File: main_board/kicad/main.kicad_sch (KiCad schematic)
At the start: 13 parts

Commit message: started bridge design
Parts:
- removed C? (x3): C, symbol Device:C
- removed D?: 1N5822, Diode_THT:D_DO-201AD_P15.24mm_Horizontal, symbol Diode:1N5822
- removed L?: L, symbol Device:L
- removed Q?: IRFB3077, Package_TO_SOT_THT:TO-220-3_Vertical, symbol 2022-lsd:IRFB3077
- removed R? (x3): R, symbol Device:R
- removed U?: LM2576S-5, Package_TO_SOT_SMD:TO-263-5_TabPin3, symbol Regulator_Switching:LM2576S-5
- removed U?: IR2133, Package_DIP:DIP-28_W15.24mm, symbol Driver_FET:IR2133
- removed U?: ATtiny13-20P, Package_DIP:DIP-8_W7.62mm, symbol MCU_Microchip_ATtiny:ATtiny13-20P
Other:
- added sheet attiny13 (attiny13.kicad_sch)
- added sheet bridge (bridge.kicad_sch)
- added sheet stepDown-24-5 (stepDown-24-5.kicad_sch)

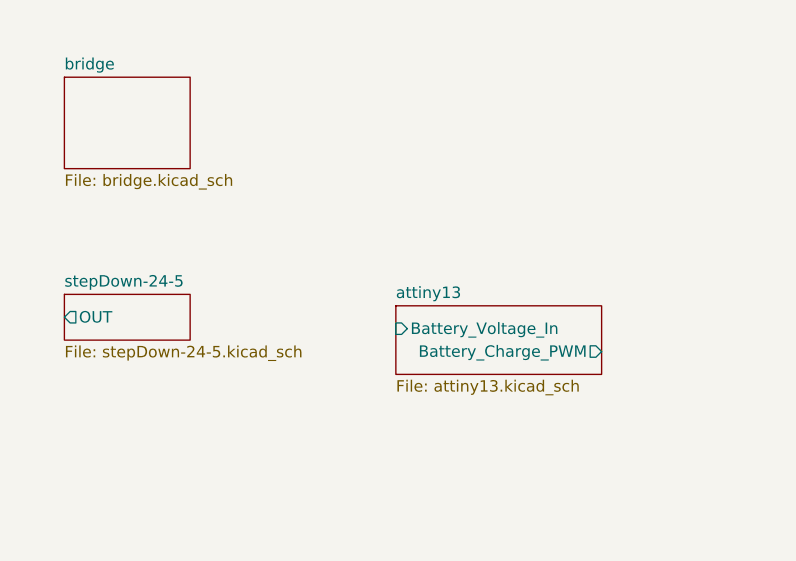
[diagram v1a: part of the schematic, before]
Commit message: changes to bridge design
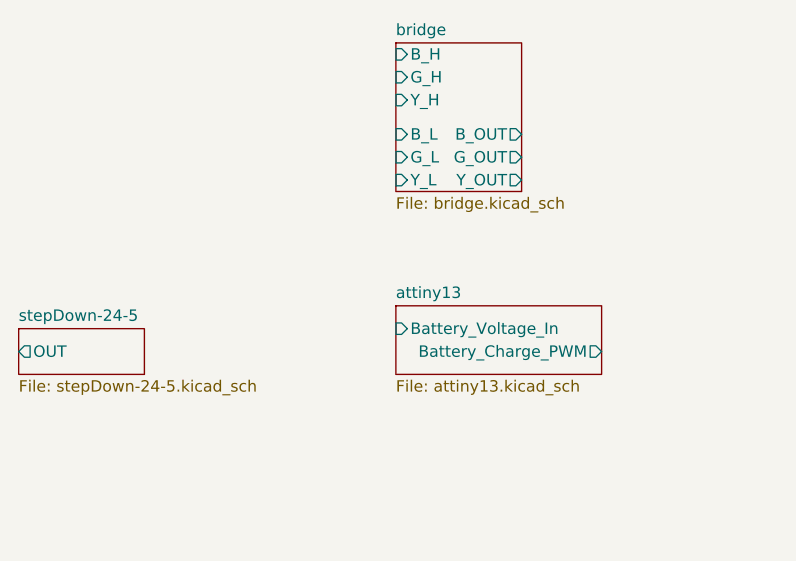
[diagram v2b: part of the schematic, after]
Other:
- sheet bridge ports: added B_H, B_L, B_OUT, G_H, G_L, G_OUT, Y_H, Y_L, Y_OUT; removed none
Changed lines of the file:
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@@
     )
   )
-  (sheet (at 163.83 156.21) (size 13.97 10.16) (fields_autoplaced)
+  (sheet (at 200.66 152.4) (size 13.97 16.51) (fields_autoplaced)
     (stroke (width 0.1524) (type solid))
     (fill (color 0 0 0 0.0000))
-    (property "Sheetname" "bridge" (at 163.83 155.4984 0)
+    (property "Sheetname" "bridge" (at 200.66 151.6884 0)
       (effects (font (size 1.27 1.27)) (justify left bottom))
     )
-    (property "Sheetfile" "bridge.kicad_sch" (at 163.83 166.9546 0)
+    (property "Sheetfile" "bridge.kicad_sch" (at 200.66 169.4946 0)
       (effects (font (size 1.27 1.27)) (justify left top))
+    )
+    (pin "G_H" input (at 200.66 156.21 180)
+      (effects (font (size 1.27 1.27)) (justify left))
+    )
+    (pin "Y_L" input (at 200.66 167.64 180)
+      (effects (font (size 1.27 1.27)) (justify left))
+    )
+    (pin "Y_OUT" output (at 214.63 167.64 0)
+      (effects (font (size 1.27 1.27)) (justify right))
+    )
+    (pin "Y_H" input (at 200.66 158.75 180)
+      (effects (font (size 1.27 1.27)) (justify left))
+    )
+    (pin "G_OUT" output (at 214.63 165.1 0)
+      (effects (font (size 1.27 1.27)) (justify right))
+    )
+    (pin "G_L" input (at 200.66 165.1 180)
+      (effects (font (size 1.27 1.27)) (justify left))
+    )
+    (pin "B_L" input (at 200.66 162.56 180)
+      (effects (font (size 1.27 1.27)) (justify left))
+    )
+    (pin "B_OUT" output (at 214.63 162.56 0)
+      (effects (font (size 1.27 1.27)) (justify right))
+    )
+    (pin "B_H" input (at 200.66 153.67 180)
+      (effects (font (size 1.27 1.27)) (justify left))
     )
     (instances
@@
     )
   )
-  (sheet (at 163.83 180.34) (size 13.97 5.08) (fields_autoplaced)
+  (sheet (at 158.75 184.15) (size 13.97 5.08) (fields_autoplaced)
     (stroke (width 0.1524) (type solid))
     (fill (color 0 0 0 0.0000))
-    (property "Sheetname" "stepDown-24-5" (at 163.83 179.6284 0)
+    (property "Sheetname" "stepDown-24-5" (at 158.75 183.4384 0)
       (effects (font (size 1.27 1.27)) (justify left bottom))
     )
-    (property "Sheetfile" "stepDown-24-5.kicad_sch" (at 163.83 186.0046 0)
+    (property "Sheetfile" "stepDown-24-5.kicad_sch" (at 158.75 189.8146 0)
       (effects (font (size 1.27 1.27)) (justify left top))
     )
-    (pin "OUT" output (at 163.83 182.88 180)
+    (pin "OUT" output (at 158.75 186.69 180)
       (effects (font (size 1.27 1.27)) (justify left))
     )

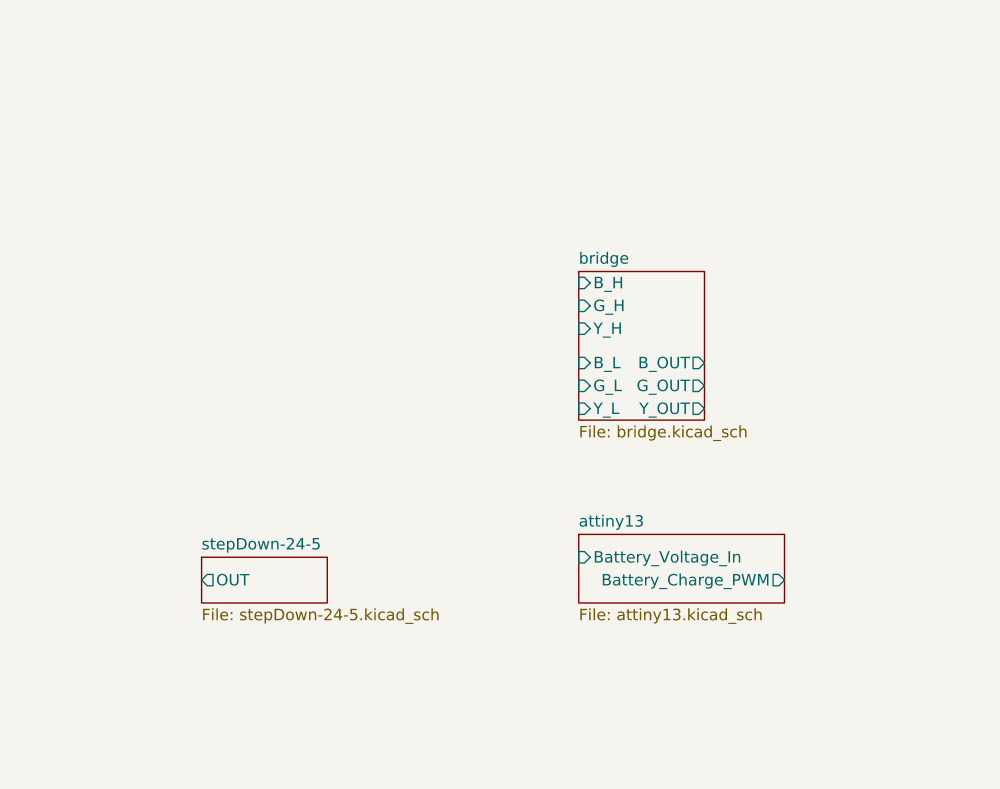
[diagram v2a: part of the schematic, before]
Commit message: added bridge driver stub
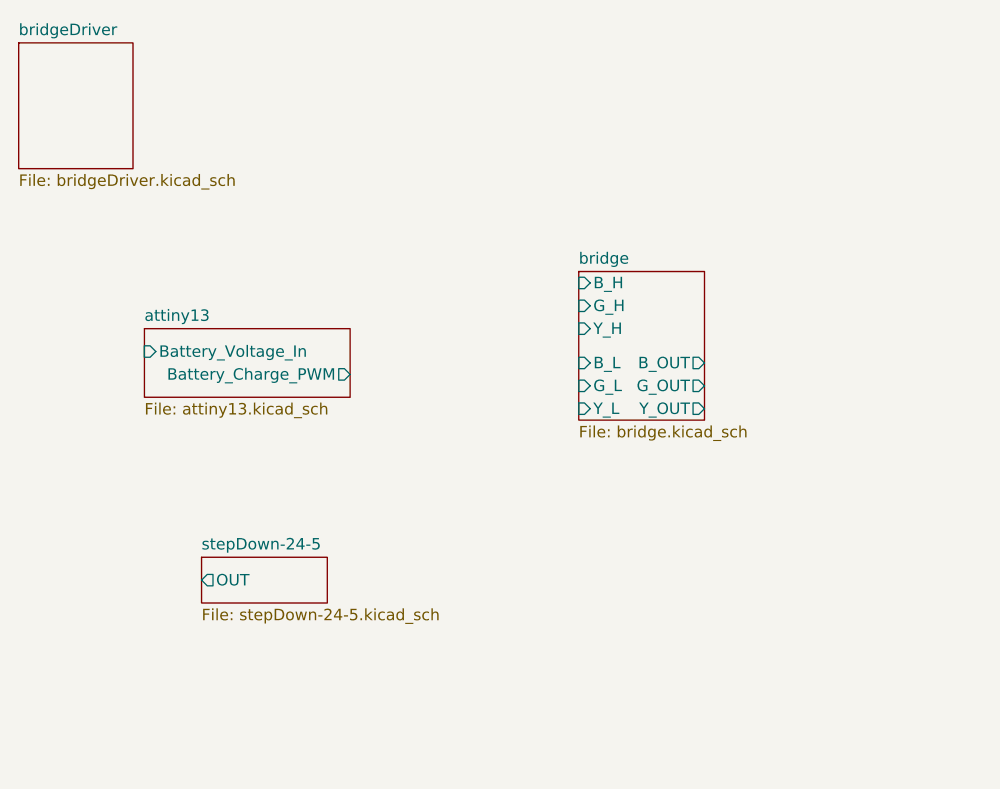
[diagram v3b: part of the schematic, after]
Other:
- added sheet bridgeDriver (bridgeDriver.kicad_sch)
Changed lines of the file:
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@@
     )
   )
-  (sheet (at 200.66 181.61) (size 22.86 7.62) (fields_autoplaced)
+  (sheet (at 152.4 158.75) (size 22.86 7.62) (fields_autoplaced)
     (stroke (width 0.1524) (type solid))
     (fill (color 0 0 0 0.0000))
-    (property "Sheetname" "attiny13" (at 200.66 180.8984 0)
+    (property "Sheetname" "attiny13" (at 152.4 158.0384 0)
       (effects (font (size 1.27 1.27)) (justify left bottom))
     )
-    (property "Sheetfile" "attiny13.kicad_sch" (at 200.66 189.8146 0)
+    (property "Sheetfile" "attiny13.kicad_sch" (at 152.4 166.9546 0)
       (effects (font (size 1.27 1.27)) (justify left top))
     )
-    (pin "Battery_Charge_PWM" output (at 223.52 186.69 0)
+    (pin "Battery_Charge_PWM" output (at 175.26 163.83 0)
       (effects (font (size 1.27 1.27)) (justify right))
     )
-    (pin "Battery_Voltage_In" input (at 200.66 184.15 180)
+    (pin "Battery_Voltage_In" input (at 152.4 161.29 180)
       (effects (font (size 1.27 1.27)) (justify left))
     )
@@
       )
     )
+  )
+  (sheet (at 138.43 127) (size 12.7 13.97) (fields_autoplaced)
+    (stroke (width 0.1524) (type solid))
+    (fill (color 0 0 0 0.0000))
+    (property "Sheetname" "bridgeDriver" (at 138.43 126.2884 0)
+      (effects (font (size 1.27 1.27)) (justify left bottom))
+    )
+    (property "Sheetfile" "bridgeDriver.kicad_sch" (at 138.43 141.5546 0)
+      (effects (font (size 1.27 1.27)) (justify left top))
+    )
+    (instances
+      (project "main"
+        (path "/9139d8e7-a5dc-421f-9a12-f77d83384a16" (page "5"))
+      )
+    )

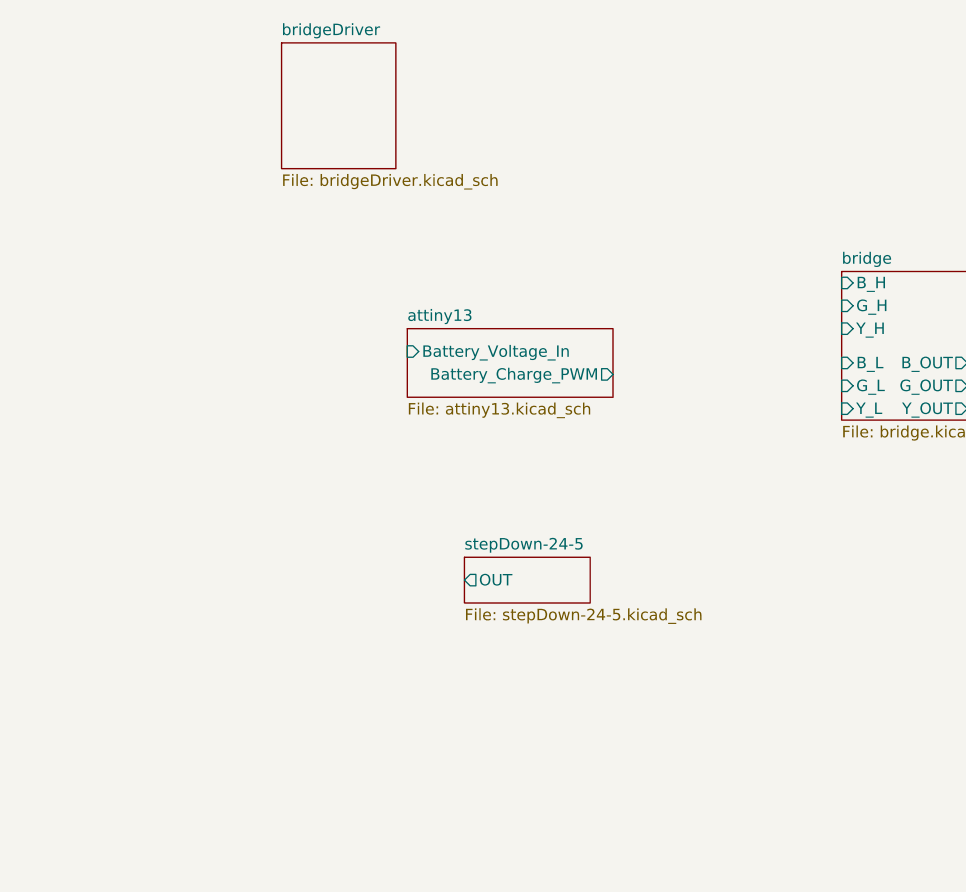
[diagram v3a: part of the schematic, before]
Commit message: added hierarchy for 15v stepdown
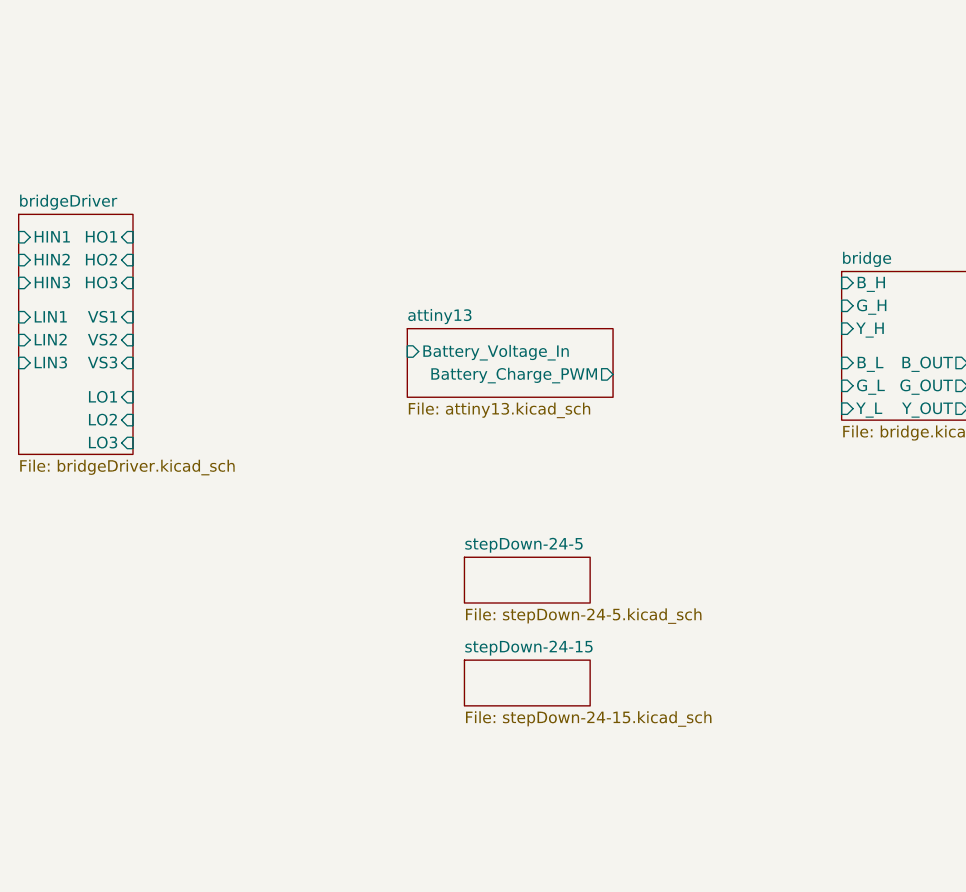
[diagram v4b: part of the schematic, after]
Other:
- added sheet stepDown-24-15 (stepDown-24-15.kicad_sch)
- sheet bridgeDriver ports: added HIN1, HIN2, HIN3, HO1, HO2, HO3, LIN1, LIN2, LIN3, LO1, LO2, LO3, VS1, VS2, VS3; removed none
- sheet stepDown-24-5 ports: added none; removed OUT
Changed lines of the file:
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@@
+    )
+  )
+  (sheet (at 158.75 195.58) (size 13.97 5.08) (fields_autoplaced)
+    (stroke (width 0.1524) (type solid))
+    (fill (color 0 0 0 0.0000))
+    (property "Sheetname" "stepDown-24-15" (at 158.75 194.8684 0)
+      (effects (font (size 1.27 1.27)) (justify left bottom))
+    )
+    (property "Sheetfile" "stepDown-24-15.kicad_sch" (at 158.75 201.2446 0)
+      (effects (font (size 1.27 1.27)) (justify left top))
+    )
+    (instances
+      (project "main"
+        (path "/9139d8e7-a5dc-421f-9a12-f77d83384a16" (page "6"))
+      )
     )
   )
@@
     (property "Sheetfile" "stepDown-24-5.kicad_sch" (at 158.75 189.8146 0)
       (effects (font (size 1.27 1.27)) (justify left top))
-    )
-    (pin "OUT" output (at 158.75 186.69 180)
-      (effects (font (size 1.27 1.27)) (justify left))
     )
     (instances
@@
     )
   )
-  (sheet (at 138.43 127) (size 12.7 13.97) (fields_autoplaced)
+  (sheet (at 109.22 146.05) (size 12.7 26.67) (fields_autoplaced)
     (stroke (width 0.1524) (type solid))
     (fill (color 0 0 0 0.0000))
-    (property "Sheetname" "bridgeDriver" (at 138.43 126.2884 0)
+    (property "Sheetname" "bridgeDriver" (at 109.22 145.3384 0)
       (effects (font (size 1.27 1.27)) (justify left bottom))
     )
-    (property "Sheetfile" "bridgeDriver.kicad_sch" (at 138.43 141.5546 0)
+    (property "Sheetfile" "bridgeDriver.kicad_sch" (at 109.22 173.3046 0)
       (effects (font (size 1.27 1.27)) (justify left top))
     )
+    (pin "HIN1" input (at 109.22 148.59 180)
+      (effects (font (size 1.27 1.27)) (justify left))
+    )
+    (pin "HIN3" input (at 109.22 153.67 180)
+      (effects (font (size 1.27 1.27)) (justify left))
+    )
+    (pin "LIN1" input (at 109.22 157.48 180)
+      (effects (font (size 1.27 1.27)) (justify left))
+    )
+    (pin "HIN2" input (at 109.22 151.13 180)
+      (effects (font (size 1.27 1.27)) (justify left))
+    )
+    (pin "LIN2" input (at 109.22 160.02 180)
+      (effects (font (size 1.27 1.27)) (justify left))
+    )
+    (pin "LIN3" input (at 109.22 162.56 180)
+      (effects (font (size 1.27 1.27)) (justify left))
+    )
+    (pin "VS3" input (at 121.92 162.56 0)
+      (effects (font (size 1.27 1.27)) (justify right))
+    )
+    (pin "LO1" input (at 121.92 166.37 0)
+      (effects (font (size 1.27 1.27)) (justify right))
+    )
+    (pin "LO3" input (at 121.92 171.45 0)
+      (effects (font (size 1.27 1.27)) (justify right))
+    )
+    (pin "LO2" input (at 121.92 168.91 0)
+      (effects (font (size 1.27 1.27)) (justify right))
+    )
+    (pin "HO3" input (at 121.92 153.67 0)
+      (effects (font (size 1.27 1.27)) (justify right))
+    )
+    (pin "VS1" input (at 121.92 157.48 0)
+      (effects (font (size 1.27 1.27)) (justify right))
+    )
+    (pin "VS2" input (at 121.92 160.02 0)
+      (effects (font (size 1.27 1.27)) (justify right))
+    )
+    (pin "HO2" input (at 121.92 151.13 0)
+      (effects (font (size 1.27 1.27)) (justify right))
+    )
+    (pin "HO1" input (at 121.92 148.59 0)
+      (effects (font (size 1.27 1.27)) (justify right))
+    )
     (instances

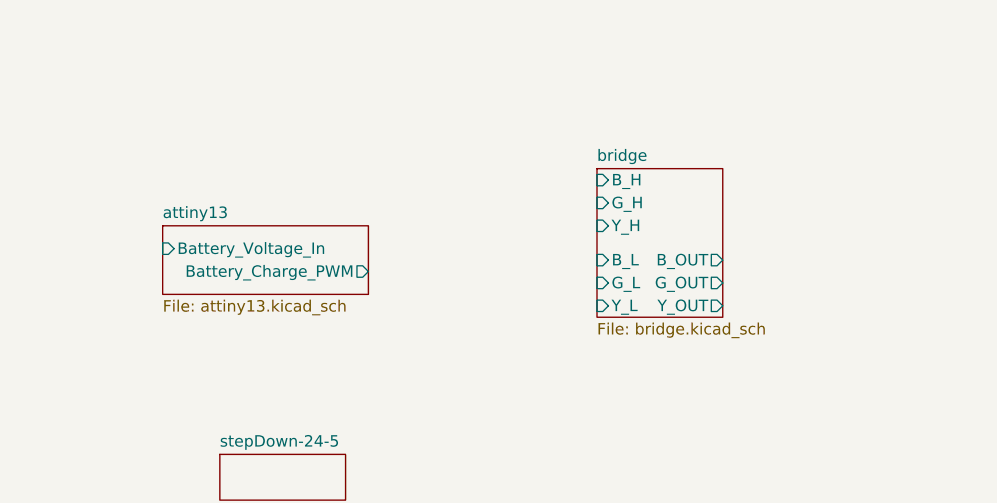
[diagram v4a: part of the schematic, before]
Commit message: implemented 15v stepdown
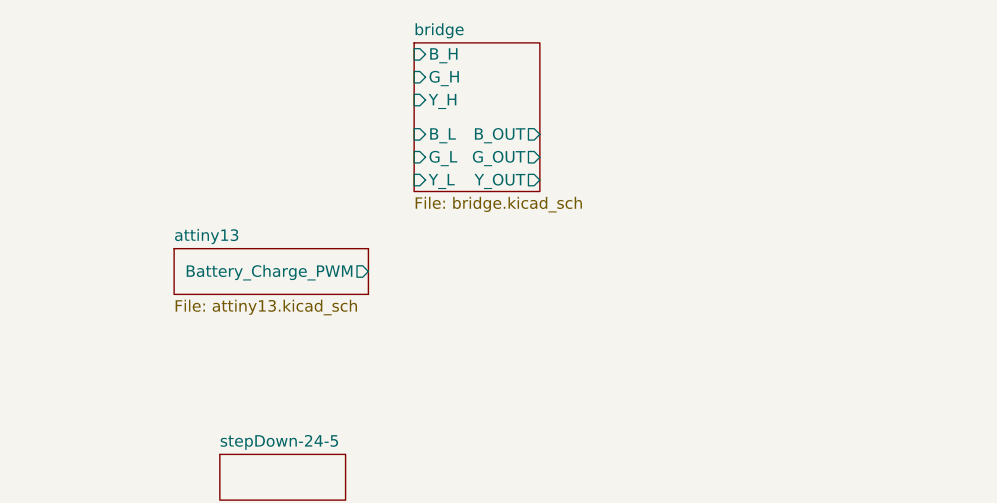
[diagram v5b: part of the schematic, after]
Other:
- sheet attiny13 ports: added none; removed Battery_Voltage_In
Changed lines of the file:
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@@
     )
   )
-  (sheet (at 200.66 152.4) (size 13.97 16.51) (fields_autoplaced)
+  (sheet (at 180.34 138.43) (size 13.97 16.51) (fields_autoplaced)
     (stroke (width 0.1524) (type solid))
     (fill (color 0 0 0 0.0000))
-    (property "Sheetname" "bridge" (at 200.66 151.6884 0)
+    (property "Sheetname" "bridge" (at 180.34 137.7184 0)
       (effects (font (size 1.27 1.27)) (justify left bottom))
     )
-    (property "Sheetfile" "bridge.kicad_sch" (at 200.66 169.4946 0)
+    (property "Sheetfile" "bridge.kicad_sch" (at 180.34 155.5246 0)
       (effects (font (size 1.27 1.27)) (justify left top))
     )
-    (pin "G_H" input (at 200.66 156.21 180)
+    (pin "G_H" input (at 180.34 142.24 180)
       (effects (font (size 1.27 1.27)) (justify left))
     )
-    (pin "Y_L" input (at 200.66 167.64 180)
+    (pin "Y_L" input (at 180.34 153.67 180)
       (effects (font (size 1.27 1.27)) (justify left))
     )
-    (pin "Y_OUT" output (at 214.63 167.64 0)
+    (pin "Y_OUT" output (at 194.31 153.67 0)
       (effects (font (size 1.27 1.27)) (justify right))
     )
-    (pin "Y_H" input (at 200.66 158.75 180)
+    (pin "Y_H" input (at 180.34 144.78 180)
       (effects (font (size 1.27 1.27)) (justify left))
     )
-    (pin "G_OUT" output (at 214.63 165.1 0)
+    (pin "G_OUT" output (at 194.31 151.13 0)
       (effects (font (size 1.27 1.27)) (justify right))
     )
-    (pin "G_L" input (at 200.66 165.1 180)
+    (pin "G_L" input (at 180.34 151.13 180)
       (effects (font (size 1.27 1.27)) (justify left))
     )
-    (pin "B_L" input (at 200.66 162.56 180)
+    (pin "B_L" input (at 180.34 148.59 180)
       (effects (font (size 1.27 1.27)) (justify left))
     )
-    (pin "B_OUT" output (at 214.63 162.56 0)
+    (pin "B_OUT" output (at 194.31 148.59 0)
       (effects (font (size 1.27 1.27)) (justify right))
     )
-    (pin "B_H" input (at 200.66 153.67 180)
+    (pin "B_H" input (at 180.34 139.7 180)
       (effects (font (size 1.27 1.27)) (justify left))
     )
@@
     )
   )
-  (sheet (at 152.4 158.75) (size 22.86 7.62) (fields_autoplaced)
+  (sheet (at 153.67 161.29) (size 21.59 5.08) (fields_autoplaced)
     (stroke (width 0.1524) (type solid))
     (fill (color 0 0 0 0.0000))
-    (property "Sheetname" "attiny13" (at 152.4 158.0384 0)
+    (property "Sheetname" "attiny13" (at 153.67 160.5784 0)
       (effects (font (size 1.27 1.27)) (justify left bottom))
     )
-    (property "Sheetfile" "attiny13.kicad_sch" (at 152.4 166.9546 0)
+    (property "Sheetfile" "attiny13.kicad_sch" (at 153.67 166.9546 0)
       (effects (font (size 1.27 1.27)) (justify left top))
     )
@@
       (effects (font (size 1.27 1.27)) (justify right))
     )
-    (pin "Battery_Voltage_In" input (at 152.4 161.29 180)
-      (effects (font (size 1.27 1.27)) (justify left))
-    )
     (instances
